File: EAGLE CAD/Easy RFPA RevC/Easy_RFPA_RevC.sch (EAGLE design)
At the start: 287 parts, among them IC1 LM741D, IC2 LM741D, IC3 LM393D, IC5 74AHC1G00DBV, IC6 74LS74D, IC7 74AHC1G86DBV, J401 HDR_2X1282836-1282836-1, J402 KK_PCFAN, Q1 IRF630, Q101 IRF520N, Q102 IRF630, Q2 MOSFET_NBSS123SOT23, Q201 IRF630, Q202 IRF630, Q3 NPNMMBT3904SOT23_BEC, Q301 MOSFET_NBSS123SOT23, Q302 PNPSOT23_BEC, Q303 NPNMMBT3904SOT23_BEC, Q4 PNPSOT23_BEC, SW1 SPST_NO_TACT_RA43125608371643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, SW2 SPST_NO_TACT_RA43125608371643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, T1 HP1_TRAFO, T102 HP4_TRAFO, U1 OPAMP_QUADTLV274IDSOIC14, U302 OPAMP_QUADTLV274IDSOIC14, U401 LDO_3TERMMC78M12CTGTO220_VERT, U402 LDO_3TERMMC78M05CTGTO220_VERT, X1 1-227161-0, X2 1-227161-0, X4 1-227161-0, X402 HEATSINK_OMNI_DUALOMNI-UNI-30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

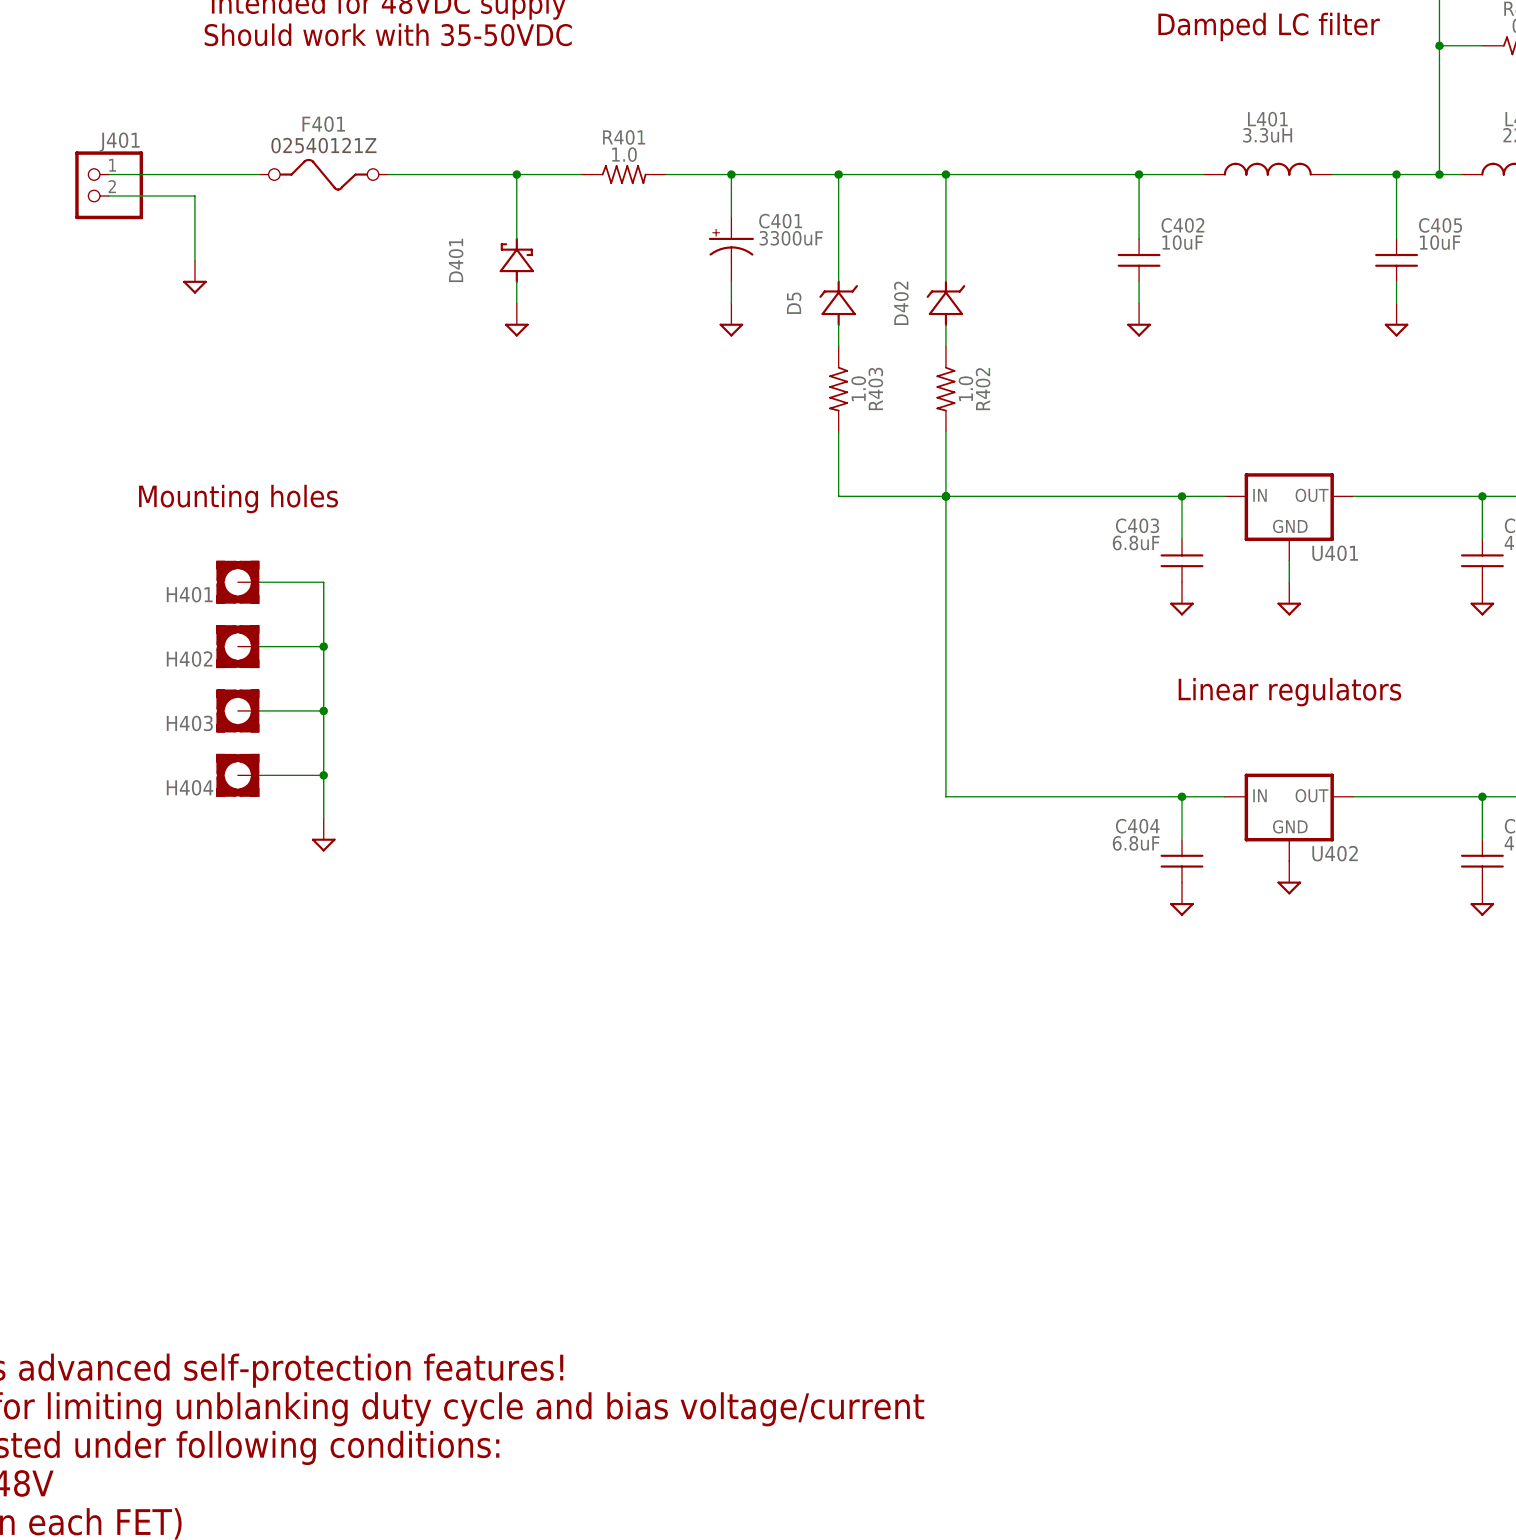
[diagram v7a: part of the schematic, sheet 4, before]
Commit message: 24V regulator
Add discrete 24V linear regulator in schematic
Using one of my TO220 FETs for the pass device for now
Added TL431 to VREF library
Also added two more mounting holes to board
And the footprint for a clip-on TO-220 heatsink
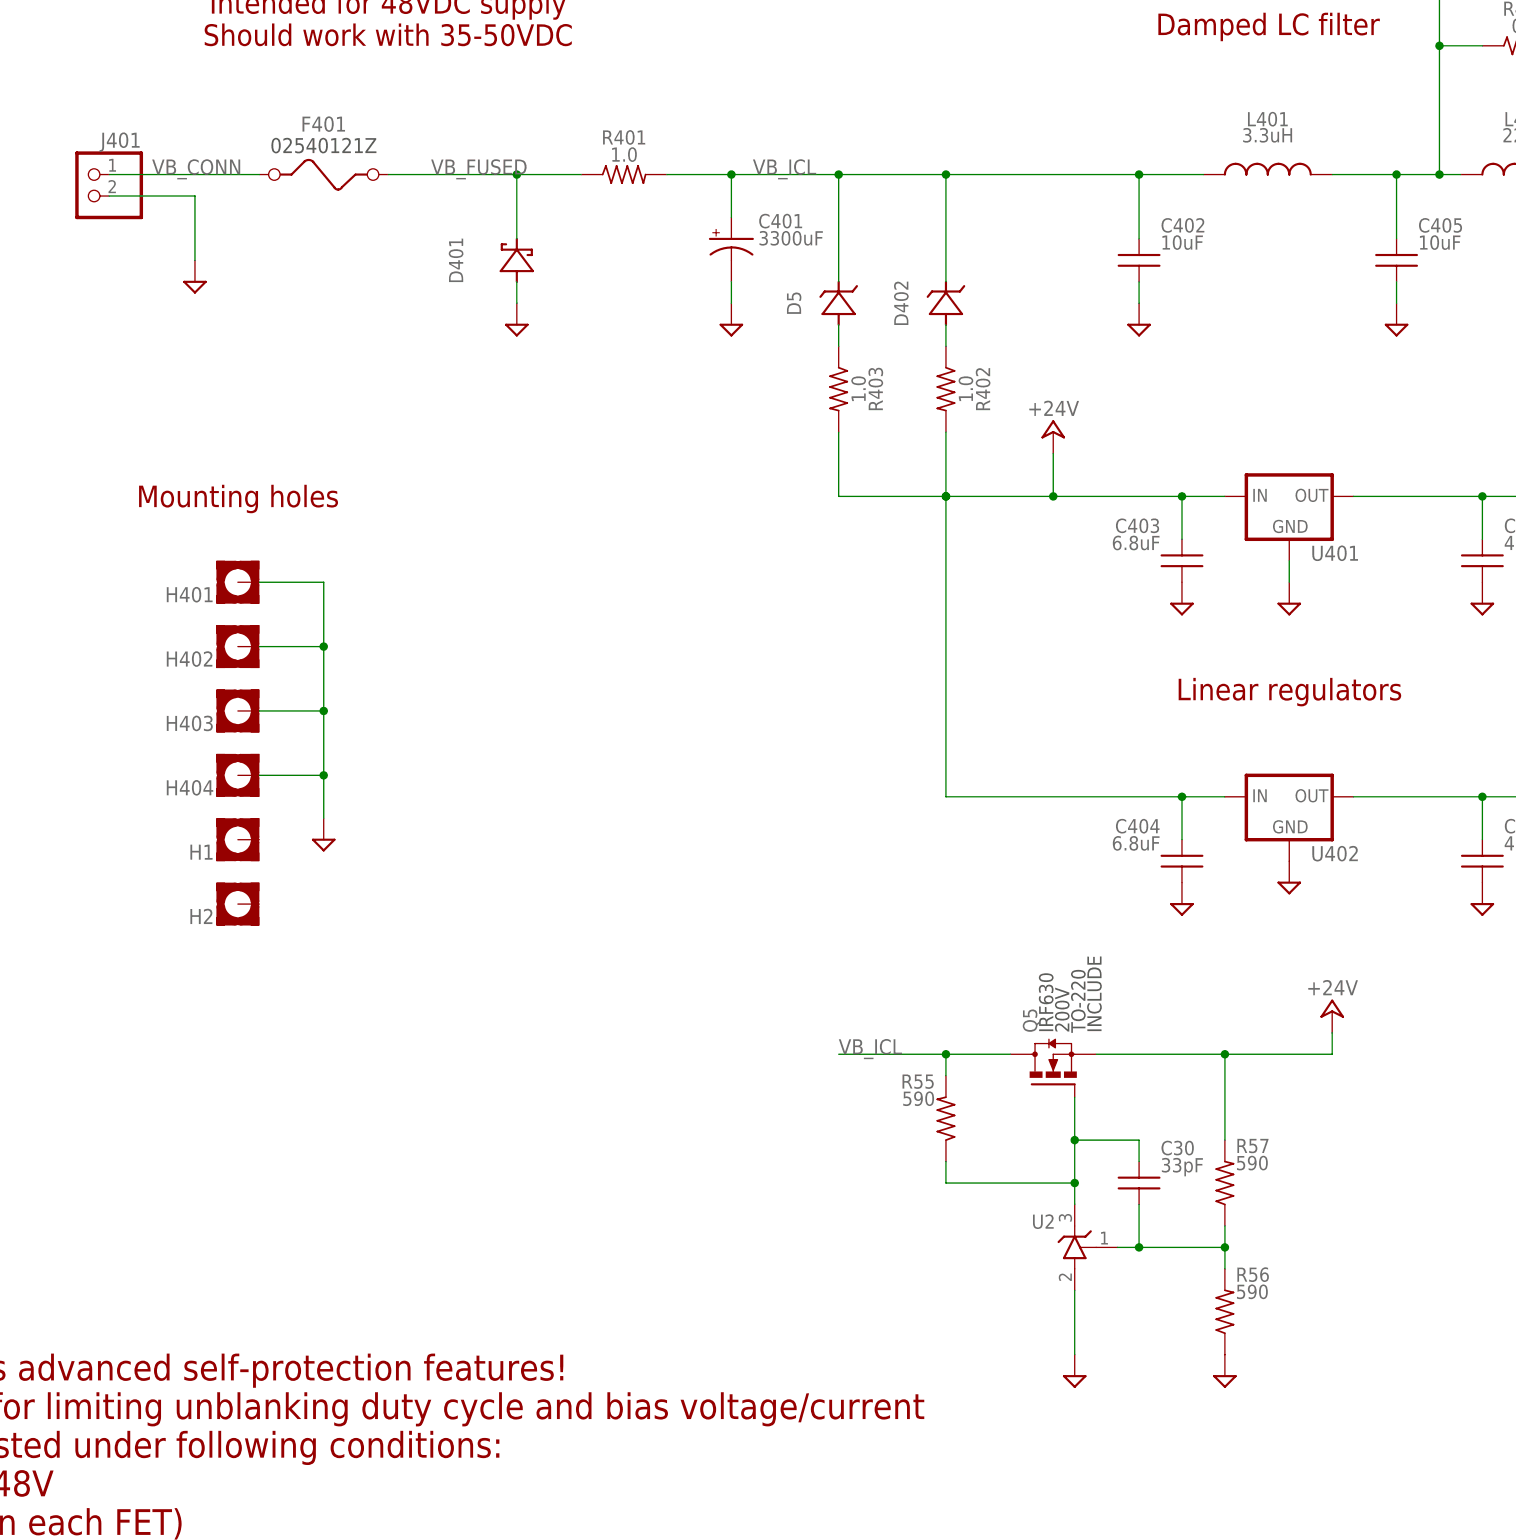
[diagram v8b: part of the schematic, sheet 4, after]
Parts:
- added C30: 33pF, MDT_C:CGEN0805_IPC
- added H1, H2: MOUNT-PAD-SQUARE3.2, holes:MOUNT-PAD-SQUARE3.2
- added Q5: IRF630, MDT_TRANS:MOSFET_NIRF630TO-220-VERT
- added R55, R56, R57: 590, MDT_R:RGEN0805_IPC
- added U2: ADJ_ZENERTL431AILPRAGTO-92-LPRE, MDT_VREF:ADJ_ZENERTL431AILPRAGTO-92-LPRE
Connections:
- net N$44 renamed VB_FUSED
- net N$45 renamed VB_CONN
- removed net N$43: C403.1, C404.1, R402.2, R403.2, U401.IN, U402.IN
- removed net N$46: C401.+, C402.1, D402.C1, D5.C1, L401.1, R401.2
- new net N$91: C30.2, R56.1, R57.2, U2.R
- new net N$92: C30.1, Q5.G, R55.2, U2.C
- new net VB_ICL: C401.+, C402.1, D402.C1, D5.C1, L401.1, Q5.D, R401.2, R55.1
- net +24V: now also C403.1, C404.1, Q5.S, R402.2, R403.2, R57.1, U401.IN, U402.IN
- net GND: now also R56.2, U2.A
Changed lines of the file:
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@@
 </part>
 <part name="SUPPLY52" library="supply2" deviceset="GND" device=""/>
+<part name="Q5" library="MDT_TRANS" deviceset="MOSFET_N" device="TO-220-VERT" technology="IRF630" value="IRF630">
+<variant name="IRF520N_20W" populate="no"/>
+</part>
+<part name="U2" library="MDT_VREF" deviceset="ADJ_ZENER" device="TO-92-LPRE" technology="TL431AILPRAG"/>
+<part name="R56" library="MDT_R" deviceset="R" device="0805_IPC" technology="GEN" value="590"/>
+<part name="R57" library="MDT_R" deviceset="R" device="0805_IPC" technology="GEN" value="590"/>
+<part name="C30" library="MDT_C" deviceset="C" device="0805_IPC" technology="GEN" value="33pF">
+<attribute name="VOLTAGE" value="50V"/>
+</part>
+<part name="SUPPLY53" library="supply2" deviceset="GND" device=""/>
+<part name="SUPPLY54" library="supply2" deviceset="GND" device=""/>
+<part name="P+23" library="supply1" deviceset="+24V" device=""/>
+<part name="P+24" library="supply1" deviceset="+24V" device=""/>
+<part name="R55" library="MDT_R" deviceset="R" device="0805_IPC" technology="GEN" value="590"/>
+<part name="H1" library="holes" deviceset="MOUNT-PAD-SQUARE" device="3.2">
+<attribute name="BOM" value="EXCLUDE"/>
+</part>
+<part name="H2" library="holes" deviceset="MOUNT-PAD-SQUARE" device="3.2">
+<attribute name="BOM" value="EXCLUDE"/>
+</part>
 </parts>
 <sheets>
@@
 <instance part="X3" gate="G$1" x="350.52" y="78.74"/>
 <instance part="X5" gate="G$1" x="365.76" y="73.66"/>
+<instance part="Q5" gate="G$1" x="170.18" y="71.12" rot="R90"/>
+<instance part="U2" gate="G$1" x="172.72" y="48.26" rot="MR0"/>
+<instance part="R56" gate="G$1" x="190.5" y="40.64"/>
+<instance part="R57" gate="G$1" x="190.5" y="55.88"/>
+<instance part="C30" gate="G$1" x="180.34" y="55.88"/>
+<instance part="SUPPLY53" gate="GND" x="190.5" y="33.02" smashed="yes"/>
+<instance part="SUPPLY54" gate="GND" x="172.72" y="33.02" smashed="yes"/>
+<instance part="P+23" gate="1" x="203.2" y="76.2" smashed="yes">
+<attribute name="VALUE" x="203.2" y="78.105" size="1.778" layer="96" align="bottom-center"/>
+</instance>
+<instance part="P+24" gate="1" x="170.18" y="144.78" smashed="yes">
+<attribute name="VALUE" x="170.18" y="146.685" size="1.778" layer="96" align="bottom-center"/>
+</instance>
+<instance part="R55" gate="G$1" x="157.48" y="63.5" rot="MR0"/>
+<instance part="H1" gate="G$1" x="73.66" y="96.52" smashed="yes" rot="R180">
+<attribute name="BOM" x="73.66" y="96.52" size="1.778" layer="96" rot="R180" display="off"/>
+<attribute name="NAME" x="70.866" y="95.9358" size="1.778" layer="95" rot="R180"/>
+</instance>
+<instance part="H2" gate="G$1" x="73.66" y="88.9" smashed="yes" rot="R180">
+<attribute name="BOM" x="73.66" y="88.9" size="1.778" layer="96" rot="R180" display="off"/>
+<attribute name="NAME" x="70.866" y="88.3158" size="1.778" layer="95" rot="R180"/>
+</instance>
 </instances>
 <busses>
@@
 <pinref part="LED402" gate="G$1" pin="C"/>
 </segment>
+<segment>
+<pinref part="R56" gate="G$1" pin="2"/>
+<pinref part="SUPPLY53" gate="GND" pin="GND"/>
+</segment>
+<segment>
+<pinref part="U2" gate="G$1" pin="A"/>
+<pinref part="SUPPLY54" gate="GND" pin="GND"/>
+<wire x1="172.72" y1="43.18" x2="172.72" y2="35.56" width="0.1524" layer="91"/>
+</segment>
 </net>
 <net name="+12V" class="0">
@@
 </segment>
 </net>
-<net name="N$43" class="0">
-<segment>
-<pinref part="U401" gate="G$1" pin="IN"/>
-<wire x1="190.5" y1="137.16" x2="185.42" y2="137.16" width="0.1524" layer="91"/>
-<pinref part="R402" gate="G$1" pin="2"/>
-<wire x1="185.42" y1="137.16" x2="157.48" y2="137.16" width="0.1524" layer="91"/>
-<wire x1="157.48" y1="137.16" x2="157.48" y2="144.78" width="0.1524" layer="91"/>
-<wire x1="185.42" y1="132.08" x2="185.42" y2="137.16" width="0.1524" layer="91"/>
-<junction x="185.42" y="137.16"/>
-<pinref part="C403" gate="G$1" pin="1"/>
-<pinref part="U402" gate="G$1" pin="IN"/>
-<wire x1="190.5" y1="101.6" x2="185.42" y2="101.6" width="0.1524" layer="91"/>
-<pinref part="R403" gate="G$1" pin="2"/>
-<wire x1="185.42" y1="101.6" x2="157.48" y2="101.6" width="0.1524" layer="91"/>
-<wire x1="157.48" y1="101.6" x2="157.48" y2="137.16" width="0.1524" layer="91"/>
-<wire x1="157.48" y1="137.16" x2="144.78" y2="137.16" width="0.1524" layer="91"/>
-<wire x1="144.78" y1="137.16" x2="144.78" y2="144.78" width="0.1524" layer="91"/>
-<wire x1="185.42" y1="96.52" x2="185.42" y2="101.6" width="0.1524" layer="91"/>
-<junction x="185.42" y="101.6"/>
-<pinref part="C404" gate="G$1" pin="1"/>
-<junction x="157.48" y="137.16"/>
-<junction x="157.48" y="137.16"/>
-</segment>
-</net>
-<net name="N$44" class="0">
+<net name="VB_FUSED" class="0">
 <segment>
 <pinref part="D401" gate="G$1" pin="C1"/>
@@
 <pinref part="R401" gate="G$1" pin="1"/>
 <pinref part="F401" gate="G$1" pin="2"/>
-</segment>
-</net>
-<net name="N$45" class="0">
+<label x="96.52" y="175.26" size="1.778" layer="95"/>
+</segment>
+</net>
+<net name="VB_CONN" class="0">
 <segment>
 <wire x1="76.2" y1="175.26" x2="58.42" y2="175.26" width="0.1524" layer="91"/>
 <pinref part="F401" gate="G$1" pin="1"/>
 <pinref part="J401" gate="G$1" pin="1"/>
-</segment>
-</net>
-<net name="N$46" class="0">
+<label x="63.5" y="175.26" size="1.778" layer="95"/>
+</segment>
+</net>
+<net name="VB_ICL" class="0">
 <segment>
 <pinref part="R401" gate="G$1" pin="2"/>
@@
 <wire x1="144.78" y1="162.56" x2="144.78" y2="175.26" width="0.1524" layer="91"/>
 <junction x="144.78" y="175.26"/>
+<label x="134.62" y="175.26" size="1.778" layer="95"/>
+</segment>
+<segment>
+<wire x1="157.48" y1="68.58" x2="157.48" y2="71.12" width="0.1524" layer="91"/>
+<pinref part="Q5" gate="G$1" pin="D"/>
+<wire x1="157.48" y1="71.12" x2="165.1" y2="71.12" width="0.1524" layer="91"/>
+<wire x1="157.48" y1="71.12" x2="144.78" y2="71.12" width="0.1524" layer="91"/>
+<junction x="157.48" y="71.12"/>
+<label x="144.78" y="71.12" size="1.778" layer="95"/>
+<pinref part="R55" gate="G$1" pin="1"/>
 </segment>
 </net>
@@
 </segment>
 </net>
+<net name="N$91" class="0">
+<segment>
+<pinref part="U2" gate="G$1" pin="R"/>
+<wire x1="177.8" y1="48.26" x2="180.34" y2="48.26" width="0.1524" layer="91"/>
+<pinref part="R57" gate="G$1" pin="2"/>
+<wire x1="180.34" y1="48.26" x2="190.5" y2="48.26" width="0.1524" layer="91"/>
+<wire x1="190.5" y1="48.26" x2="190.5" y2="50.8" width="0.1524" layer="91"/>
+<pinref part="R56" gate="G$1" pin="1"/>
+<wire x1="190.5" y1="48.26" x2="190.5" y2="45.72" width="0.1524" layer="91"/>
+<junction x="190.5" y="48.26"/>
+<pinref part="C30" gate="G$1" pin="2"/>
+<wire x1="180.34" y1="53.34" x2="180.34" y2="48.26" width="0.1524" layer="91"/>
+<junction x="180.34" y="48.26"/>
+</segment>
+</net>
+<net name="N$92" class="0">
+<segment>
+<wire x1="157.48" y1="58.42" x2="157.48" y2="55.88" width="0.1524" layer="91"/>
+<pinref part="C30" gate="G$1" pin="1"/>
+<wire x1="180.34" y1="58.42" x2="180.34" y2="60.96" width="0.1524" layer="91"/>
+<wire x1="180.34" y1="60.96" x2="172.72" y2="60.96" width="0.1524" layer="91"/>
+<pinref part="U2" gate="G$1" pin="C"/>
+<wire x1="172.72" y1="60.96" x2="172.72" y2="55.88" width="0.1524" layer="91"/>
+<pinref part="Q5" gate="G$1" pin="G"/>
+<wire x1="172.72" y1="55.88" x2="172.72" y2="53.34" width="0.1524" layer="91"/>
+<wire x1="172.72" y1="66.04" x2="172.72" y2="60.96" width="0.1524" layer="91"/>
+<junction x="172.72" y="60.96"/>
+<wire x1="157.48" y1="55.88" x2="172.72" y2="55.88" width="0.1524" layer="91"/>
+<junction x="172.72" y="55.88"/>
+<pinref part="R55" gate="G$1" pin="2"/>
+</segment>
+</net>
+<net name="+24V" class="0">
+<segment>
+<pinref part="Q5" gate="G$1" pin="S"/>
+<pinref part="R57" gate="G$1" pin="1"/>
+<wire x1="175.26" y1="71.12" x2="190.5" y2="71.12" width="0.1524" layer="91"/>
+<wire x1="190.5" y1="71.12" x2="190.5" y2="60.96" width="0.1524" layer="91"/>
+<wire x1="190.5" y1="71.12" x2="203.2" y2="71.12" width="0.1524" layer="91"/>
+<junction x="190.5" y="71.12"/>
+<pinref part="P+23" gate="1" pin="+24V"/>
+<wire x1="203.2" y1="71.12" x2="203.2" y2="73.66" width="0.1524" layer="91"/>
+</segment>
+<segment>
+<pinref part="U401" gate="G$1" pin="IN"/>
+<wire x1="190.5" y1="137.16" x2="185.42" y2="137.16" width="0.1524" layer="91"/>
+<pinref part="R402" gate="G$1" pin="2"/>
+<wire x1="185.42" y1="137.16" x2="170.18" y2="137.16" width="0.1524" layer="91"/>
+<wire x1="170.18" y1="137.16" x2="157.48" y2="137.16" width="0.1524" layer="91"/>
+<wire x1="157.48" y1="137.16" x2="157.48" y2="144.78" width="0.1524" layer="91"/>
+<wire x1="185.42" y1="132.08" x2="185.42" y2="137.16" width="0.1524" layer="91"/>
+<junction x="185.42" y="137.16"/>
+<pinref part="C403" gate="G$1" pin="1"/>
+<pinref part="U402" gate="G$1" pin="IN"/>
+<wire x1="190.5" y1="101.6" x2="185.42" y2="101.6" width="0.1524" layer="91"/>
+<pinref part="R403" gate="G$1" pin="2"/>
+<wire x1="185.42" y1="101.6" x2="157.48" y2="101.6" width="0.1524" layer="91"/>
+<wire x1="157.48" y1="101.6" x2="157.48" y2="137.16" width="0.1524" layer="91"/>
+<wire x1="157.48" y1="137.16" x2="144.78" y2="137.16" width="0.1524" layer="91"/>
+<wire x1="144.78" y1="137.16" x2="144.78" y2="144.78" width="0.1524" layer="91"/>
+<wire x1="185.42" y1="96.52" x2="185.42" y2="101.6" width="0.1524" layer="91"/>
+<junction x="185.42" y="101.6"/>
+<pinref part="C404" gate="G$1" pin="1"/>
+<junction x="157.48" y="137.16"/>
+<junction x="157.48" y="137.16"/>
+<pinref part="P+24" gate="1" pin="+24V"/>
+<wire x1="170.18" y1="142.24" x2="170.18" y2="137.16" width="0.1524" layer="91"/>
+<junction x="170.18" y="137.16"/>
+</segment>
+</net>
